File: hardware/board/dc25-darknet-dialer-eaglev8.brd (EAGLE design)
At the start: 101.6 x 101.6 mm, 80 parts, among them SW1 RESET, X1 USB-MICROB, Y1 RESONATORSMD

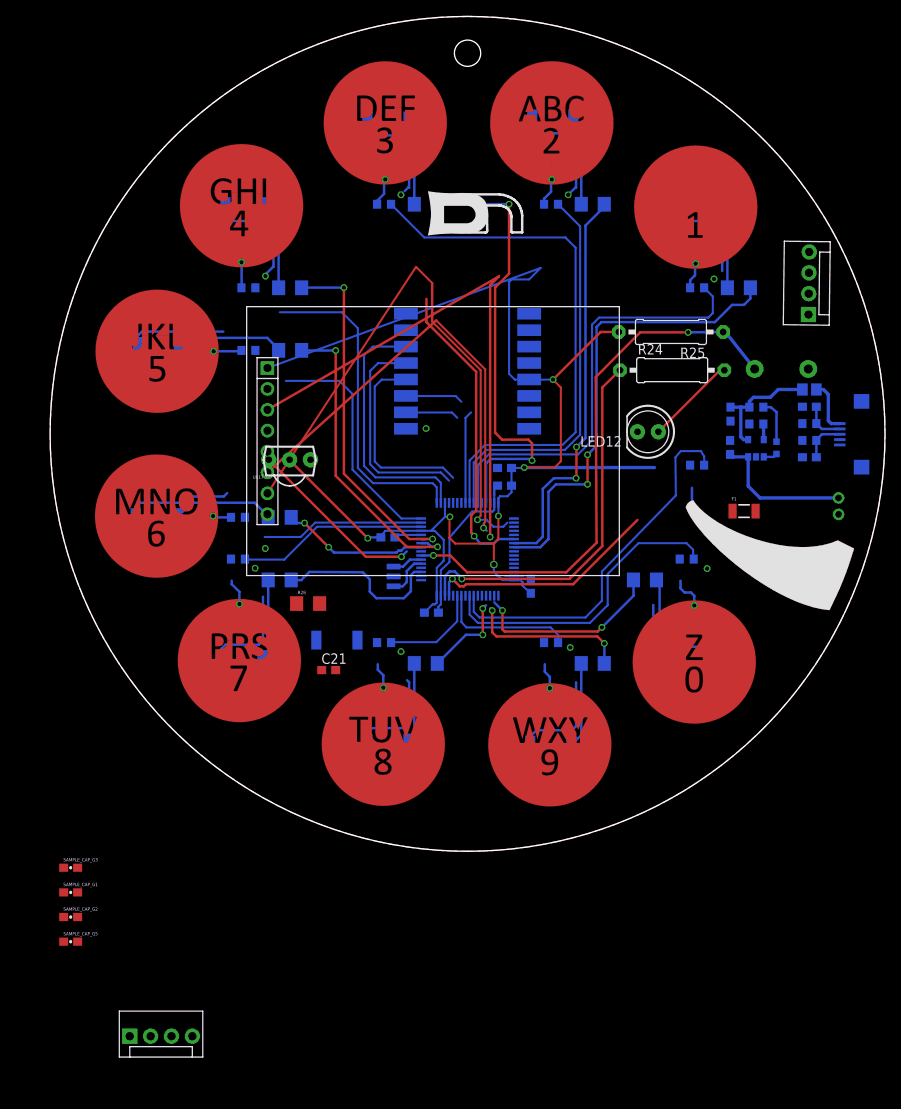
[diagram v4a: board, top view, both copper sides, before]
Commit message: Cleanup and update of schematic, added voltage regulator
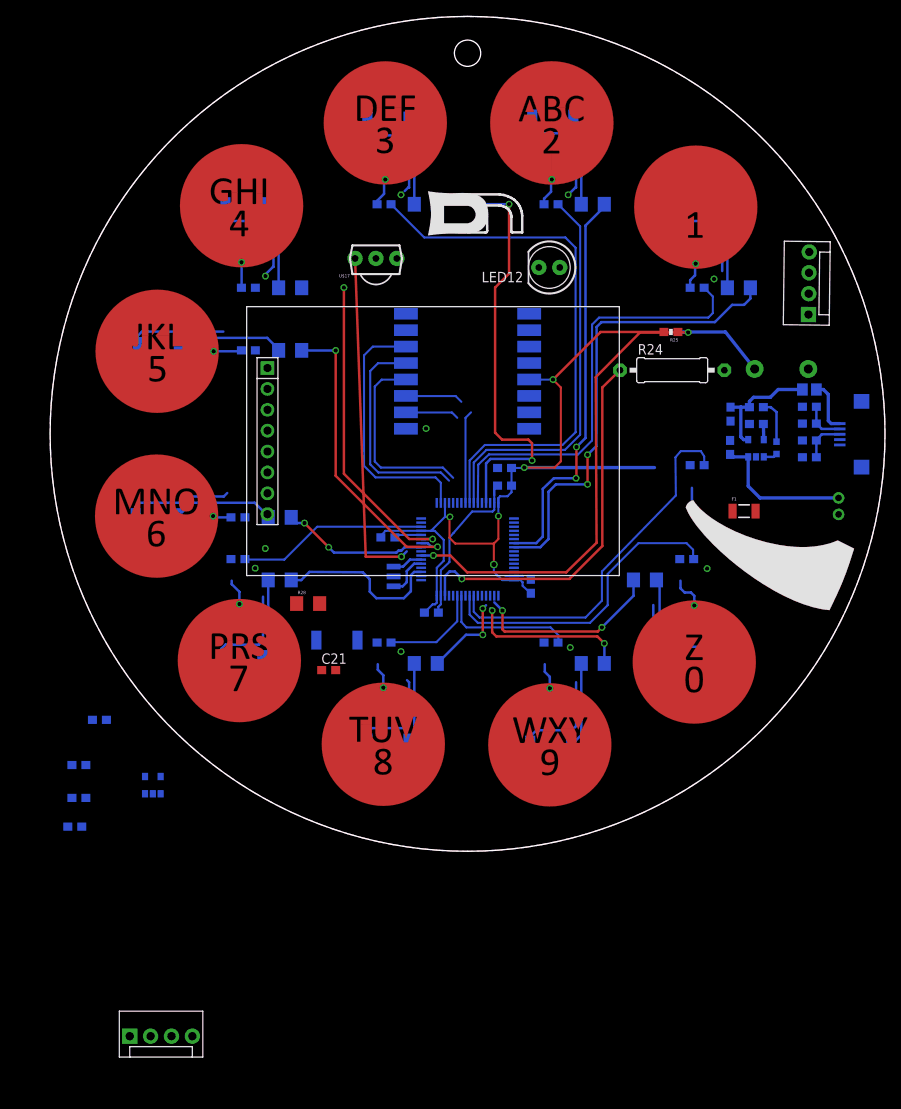
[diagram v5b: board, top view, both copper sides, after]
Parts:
- added U$19: TLV702, darknet_parts_library:SOT23-5
- C12, C13, C14: value 100nF -> 0.1uF; device SYNShop:C0603 -> darknet_parts_library:C0603
- C15: value 10nF -> 0.01uF; device SYNShop:C0603 -> darknet_parts_library:C0603
- C16, C17, C18: device SYNShop:C0603 -> darknet_parts_library:C0603
- C19, C20: value (none) -> 47pF; device SYNShop:C0603 -> darknet_parts_library:C0603
- C21: value (none) -> 1uF; device SYNShop:C0603 -> darknet_parts_library:C0603
- R1, R10, R2, R28, R3, R4, R5, R6, R7, R8, R9: device SYNShop:1206 -> darknet_parts_library:1206
- R11, R12, R13, R14, R15, R16, R17, R18, R19, R20, R21, R22, R23: device SYNShop:R0603 -> darknet_parts_library:0603-RES
- R24: device SYNShop:0309/12 -> darknet_parts_library:0309/12
- R25: device SYNShop:0309/12 -> darknet_parts_library:0603-RES
- R26, R27: value (none) -> 27; device SYNShop:R0603 -> darknet_parts_library:0603-RES
- SAMPLE_CAP_G1, SAMPLE_CAP_G2, SAMPLE_CAP_G3, SAMPLE_CAP_G5: value 10pF -> 0.047uF; device SparkFun-Capacitors:0603-CAP -> darknet_parts_library:C0603
- X1: value USB-MICROB -> 10118193-0001LF
- moved U$17 26.7 mm to (39.6, 72.2)
- moved LED12 23.3 mm to (60.8, 71.0)
- moved SAMPLE_CAP_G3 18.3 mm to (6.00, 16.0), flipped to the bottom
- moved SAMPLE_CAP_G1 15.5 mm to (3.50, 10.5), flipped to the bottom
- moved SAMPLE_CAP_G2 14.5 mm to (3.50, 6.50), flipped to the bottom
- moved SAMPLE_CAP_G5 14.0 mm to (3.00, 3.00), flipped to the bottom
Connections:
- removed net N$31: F1.2
- new net N$30: F1.2, U$19.1, U$19.3
- net GND: now also SAMPLE_CAP_G1.2, SAMPLE_CAP_G2.2, SAMPLE_CAP_G3.2, SAMPLE_CAP_G5.2, U$19.2
- net USB_DM: now also R26.2
- net USB_DP: now also R27.2
- net VCC: now also U$19.5
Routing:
- net LCD_SPI_SCK: track 71.3 -> 0.00 mm, vias 1 -> 0
- net LCD_SPI_NSS: track 65.0 -> 0.00 mm, vias 1 -> 0
- net VCC: track 166.2 -> 102.7 mm, vias 6 -> 5
- net LCD_SPI_MOSI: track 56.0 -> 0.00 mm, vias 1 -> 0
- net TSC_G1_IO4: track 39.8 -> 0.00 mm
- net LCD_RESET: track 37.3 -> 0.00 mm, vias 1 -> 0
- net TSC_G1_IO3: track 28.8 -> 0.00 mm
- net TIM_IR_CARRIER_FREQ: track 28.5 -> 0.00 mm, vias 1 -> 0
- net TSC_G1_IO2: track 19.8 -> 0.00 mm
- net IR_RCV: track 21.9 -> 41.6 mm
- net N$23: track 11.1 -> 0.00 mm
- net LED4: track 43.3 -> 38.2 mm
- net RESET: track 67.6 -> 70.1 mm

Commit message: Updated display module, added antenna design
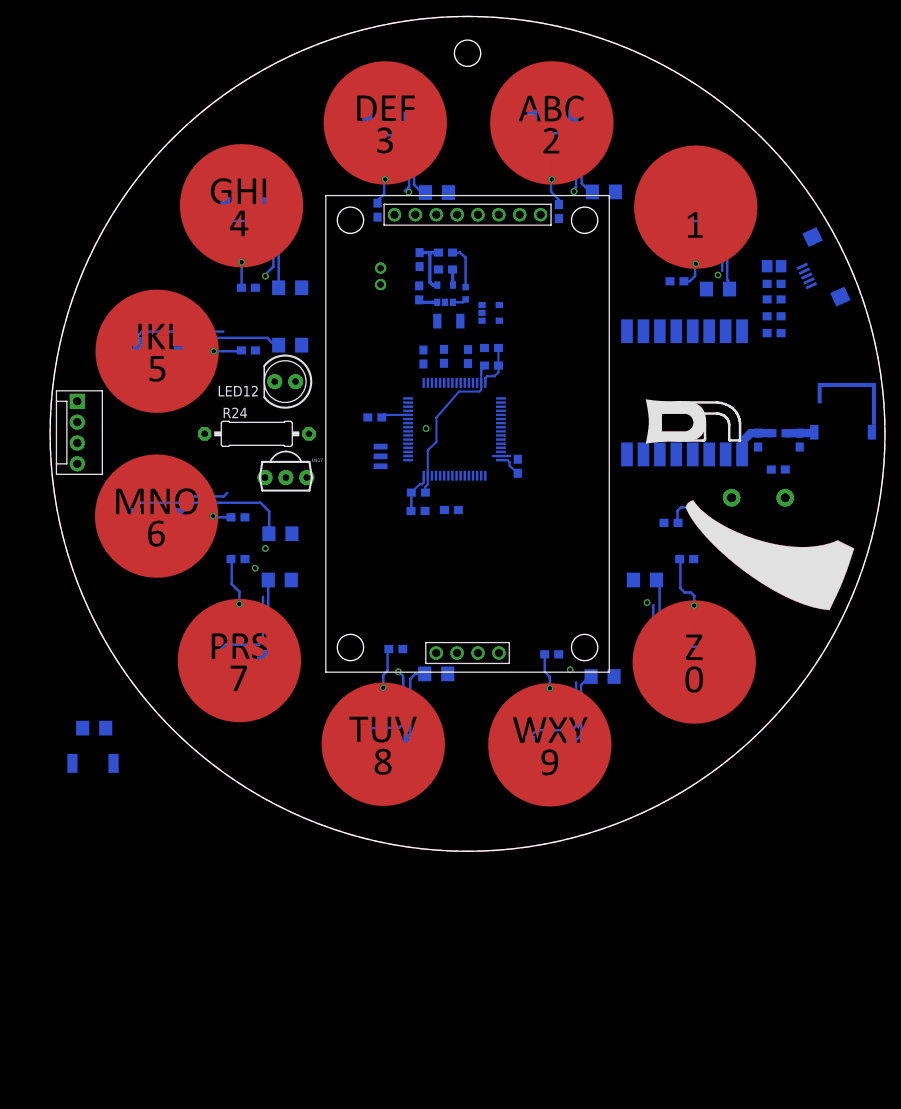
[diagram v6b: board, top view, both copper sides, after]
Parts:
- removed SD_CARD_HEADER: SD_CARD_HEADER, darknet_parts_library:SD_CARD_CONNECTOR
- removed U$12: COLOR_LCD_MODULE, darknet_parts_library:COLOR_LCD_DISPLAY
- added C1: 0.5pF, darknet_parts_library:C0603
- added L2: 10nH, darknet_parts_library:0603
- added L3: 4.7nH, darknet_parts_library:0603
- added U$21: CHIP_ANTENNA, darknet_parts_library:CHIP_ANTENNA_1.8X8MM
- added U$22: ST7735S_LCD_MODULE, darknet_parts_library:ST7735S_LCD_DISPLAY
- moved STLINK 91.4 mm to (3.31, 49.7), turned to 270 degrees
- moved U$19 70.7 mm to (53.6, 65.5), turned to 90 degrees
- moved SAMPLE_CAP_G2 69.7 mm to (47.9, 60.2), turned to 90 degrees
- moved SAMPLE_CAP_G1 65.0 mm to (45.4, 60.2), turned to 90 degrees
- moved SAMPLE_CAP_G3 63.0 mm to (50.8, 60.2), turned to 90 degrees
- moved CN1 62.4 mm to (40.2, 70.0)
- moved SAMPLE_CAP_G5 59.9 mm to (48.8, 41.5), turned to 180 degrees
- moved R24 51.1 mm to (25.1, 50.8)
- moved F1 42.7 mm to (48.5, 64.5), flipped to the bottom, turned to 180 degrees
- moved U$11 42.3 mm to (48.1, 67.8)
- moved C17 42.3 mm to (44.9, 68.0)
- moved LED11 42.3 mm to (50.6, 67.9)
- moved R22 42.3 mm to (48.1, 70.8)
- moved R23 42.3 mm to (48.1, 72.9)
- moved C18 42.3 mm to (45.0, 72.0)
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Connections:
- new net ANT: L2.1, L3.2, U$15.ANT
- new net N$31: C1.2, L2.2, U$21.P$1
- net GND: now also C1.1, L3.1, U$22.GND; no longer U$12.GND
- net LCD_BACK_LIT: now also U$22.LED; no longer U$12.LED
- net LCD_DATA_CMD: now also U$22.A0; no longer U$12.A0
- net LCD_RESET: now also U$22.RESET; no longer U$12.RESET
- net LCD_SPI_MOSI: now also U$22.SDA; no longer U$12.SDA
- net LCD_SPI_NSS: now also U$22.CS; no longer U$12.CS
- net LCD_SPI_SCK: now also U$22.SCK; no longer U$12.SCK
- net RFM69_SPI_MISO: now also U$22.SD_MISO; no longer SD_CARD_HEADER.SD_MISO
- net RFM69_SPI_MOSI: now also U$22.SD_MOSI; no longer SD_CARD_HEADER.SD_MOSI
- net RFM69_SPI_SCK: now also U$22.SD_SCK; no longer SD_CARD_HEADER.SD_SCK
- net SD_CS: now also U$22.SD_CS; no longer SD_CARD_HEADER.SD_CS
- net VCC: now also U$22.VCC; no longer U$12.VCC
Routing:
- net VCC: track 102.7 -> 13.5 mm, vias 5 -> 0
- net RESET: track 70.1 -> 0.00 mm, vias 2 -> 0
- net TSC_G3_IO1: track 66.6 -> 0.00 mm
- net LED1: track 56.6 -> 0.00 mm, vias 2 -> 0
- net LED3: track 55.1 -> 0.00 mm, vias 2 -> 0
- net TSC_G3_IO3: track 52.6 -> 0.00 mm
- net LED2: track 49.0 -> 0.00 mm, vias 2 -> 0
- net TSC_G3_IO2: track 48.4 -> 0.00 mm
- net IR_OUT: track 46.1 -> 0.00 mm, vias 1 -> 0
- net TSC_G5_IO1: track 45.1 -> 0.00 mm
- net IR_RCV: track 41.6 -> 0.00 mm, vias 1 -> 0
- net LED4: track 38.2 -> 0.03 mm, vias 2 -> 0
- net TSC_G5_IO2: track 37.7 -> 0.00 mm
- net LED5: track 37.6 -> 0.00 mm, vias 2 -> 0
- net RFM69_RESET: track 31.6 -> 0.00 mm
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
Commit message: Changed status LED for board debugging
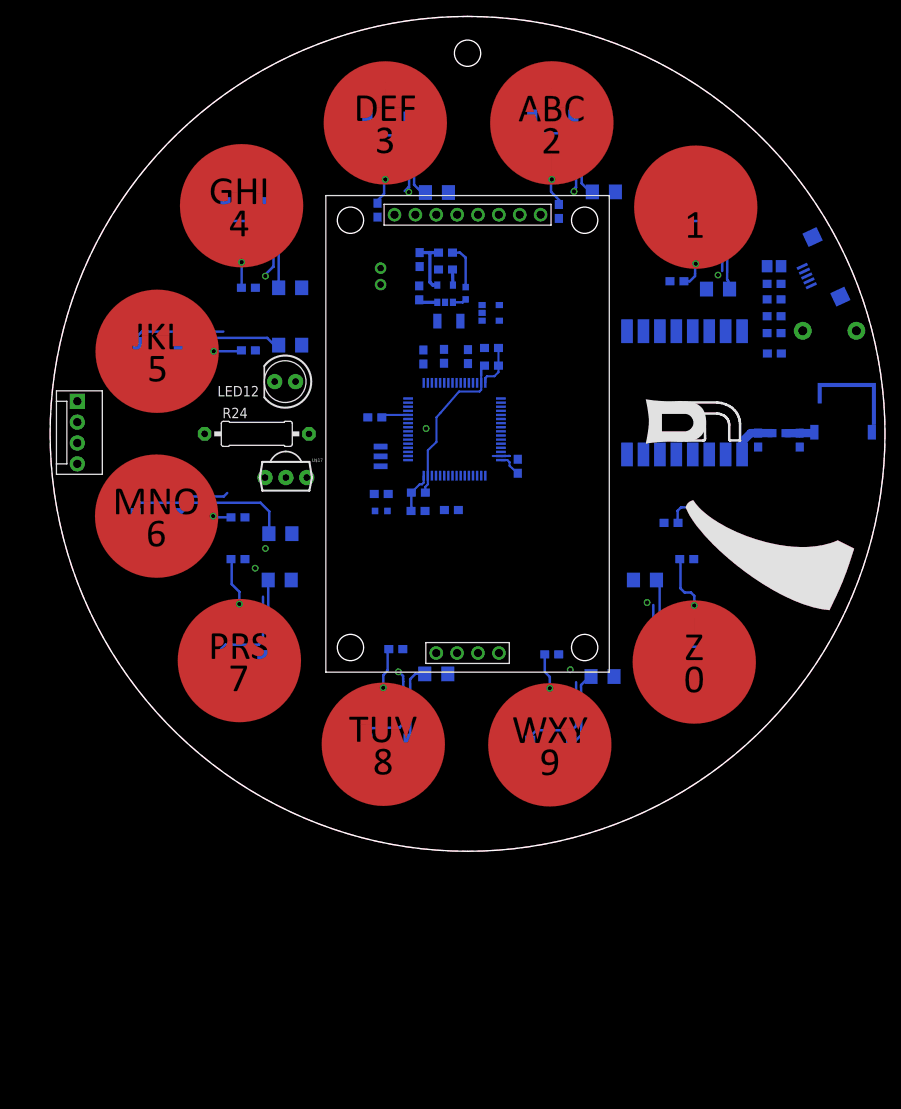
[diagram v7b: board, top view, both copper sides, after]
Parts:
- LED13: device SYNShop:GULLWING_LED -> SYNShop:LED-0603
- R28: device darknet_parts_library:1206 -> darknet_parts_library:0603-RES
- moved R28 45.1 mm to (40.3, 43.5)
- moved LED13 43.8 mm to (40.3, 41.4), turned to 90 degrees
- moved SW1 22.1 mm to (94.9, 63.3), turned to 0 degrees
- moved R25 14.1 mm to (88.1, 60.6)
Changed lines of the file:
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@@
 <element name="R24" library="darknet_parts_library" package="0309/12" value="" x="25.15" y="50.801875"/>
 <element name="CN1" library="adafruit" package="JST-PH-2-THM-RA" value="" x="40.218125" y="69.965" rot="MR270"/>
-<element name="SW1" library="SYNShop" package="TACTILE-2PIN-NARROW" value="RESET" x="86.19875" y="43.020625" rot="MR180"/>
-<element name="R25" library="darknet_parts_library" package="0603-RES" value="" x="88.609375" y="46.458125" rot="MR0"/>
+<element name="SW1" library="SYNShop" package="TACTILE-2PIN-NARROW" value="RESET" x="94.855625" y="63.341875" rot="MR0"/>
+<element name="R25" library="darknet_parts_library" package="0603-RES" value="" x="88.133125" y="60.586875" rot="MR0"/>
 <element name="R26" library="darknet_parts_library" package="0603-RES" value="27" x="88.10375" y="67.16375" rot="MR0"/>
 <element name="R27" library="darknet_parts_library" package="0603-RES" value="27" x="88.10375" y="65.11375" rot="MR0"/>
@@
 <element name="F1" library="SparkFun" package="PTC-1206" value="500uA" x="48.524375" y="64.525" rot="MR180"/>
 <element name="C21" library="darknet_parts_library" package="C0603" value="1uF" x="44.774375" y="41.4175" rot="MR0"/>
-<element name="LED13" library="SYNShop" package="GULLWING_LED" value="" x="7.71375" y="12.198125" rot="MR0"/>
-<element name="R28" library="darknet_parts_library" package="1206" value="" x="5.365" y="14.989375" rot="MR0"/>
+<element name="LED13" library="SYNShop" package="LED-0603" value="" x="40.296875" y="41.419375" rot="MR90"/>
+<element name="R28" library="darknet_parts_library" package="0603-RES" value="" x="40.29" y="43.485" rot="MR0"/>
 <element name="STLINK" library="darknet_parts_library" package="1X04" value="STLINK-V2-CONNECTOR" x="3.306875" y="49.688125" rot="R270"/>
 <element name="SAMPLE_CAP_G3" library="darknet_parts_library" package="C0603" value="0.047uF" x="50.845625" y="60.19875" rot="MR90"/>
@@
 <wire x1="42.95775" y1="21.336" x2="42.306875" y2="21.986875" width="0.3048" layer="16"/>
 <wire x1="42.306875" y1="21.986875" x2="42.306875" y2="22.06625" width="0.3048" layer="16"/>
-<wire x1="20.828" y1="23.344" x2="7.71375" y2="10.698125" width="0" layer="19" extent="16-16"/>
 </signal>
 <signal name="N$1">
@@
 <contactref element="R25" pad="1"/>
 <contactref element="SW1" pad="P$1"/>
-<wire x1="89.46265" y1="43.020625" x2="89.459375" y2="46.458125" width="0" layer="19" extent="16-16"/>
-<wire x1="43.5625" y1="50.605" x2="89.459375" y2="46.458125" width="0" layer="19" extent="16-16"/>
+<wire x1="88.983125" y1="60.586875" x2="91.591725" y2="63.341875" width="0" layer="19" extent="16-16"/>
+<wire x1="43.5625" y1="50.605" x2="88.983125" y2="60.586875" width="0" layer="19" extent="16-16"/>
 </signal>
 <signal name="VCC">
@@
 <wire x1="43.9625" y1="43.655" x2="43.9625" y2="41.455625" width="0.3048" layer="16"/>
 <wire x1="43.9625" y1="41.455625" x2="43.924375" y2="41.4175" width="0.3048" layer="16"/>
-<wire x1="54.66125" y1="64.575625" x2="59.69" y2="77.47" width="0" layer="19" extent="16-16"/>
-<wire x1="54.5625" y1="61.255" x2="54.66125" y2="64.575625" width="0" layer="19" extent="16-16"/>
+<wire x1="76.205" y1="48.295" x2="87.283125" y2="60.586875" width="0" layer="19" extent="16-16"/>
+<wire x1="56.9125" y1="46.005" x2="76.205" y2="48.295" width="0" layer="19" extent="16-16"/>
+<wire x1="52.9625" y1="57.005" x2="54.8625" y2="47.605" width="0" layer="19" extent="16-16"/>
+<wire x1="54.66125" y1="64.575625" x2="54.5625" y2="61.255" width="0" layer="19" extent="16-16"/>
 <wire x1="46.4625" y1="57.005" x2="52.9625" y2="57.005" width="0" layer="19" extent="16-16"/>
 <wire x1="43.5625" y1="53.605" x2="46.4625" y2="57.005" width="0" layer="19" extent="16-16"/>
 <wire x1="38.6625" y1="52.805" x2="43.5625" y2="53.605" width="0" layer="19" extent="16-16"/>
 <wire x1="45.4625" y1="45.705" x2="43.5625" y2="53.605" width="0" layer="19" extent="16-16"/>
-<wire x1="54.8625" y1="47.605" x2="52.9625" y2="57.005" width="0" layer="19" extent="16-16"/>
 <wire x1="28.691875" y1="45.48375" x2="38.6625" y2="52.805" width="0" layer="19" extent="16-16"/>
-<wire x1="76.205" y1="48.295" x2="56.9125" y2="46.005" width="0" layer="19" extent="16-16"/>
-<wire x1="87.759375" y1="46.458125" x2="76.205" y2="48.295" width="0" layer="19" extent="16-16"/>
+<wire x1="59.69" y1="77.47" x2="54.66125" y2="64.575625" width="0" layer="19" extent="16-16"/>
 <wire x1="3.306875" y1="54.768125" x2="28.691875" y2="45.48375" width="0" layer="19" extent="1-1"/>
 </signal>
@@
 <contactref element="U$2" pad="P2"/>
 <contactref element="R28" pad="1"/>
-<wire x1="6.765" y1="14.989375" x2="43.5625" y2="48.105" width="0" layer="19" extent="16-16"/>
+<wire x1="41.14" y1="43.485" x2="43.5625" y2="48.105" width="0" layer="19" extent="16-16"/>
 </signal>
 <signal name="TSC_G5_IO4">
@@
 <contactref element="LED13" pad="A"/>
 <contactref element="R28" pad="2"/>
-<wire x1="2.71375" y1="10.698125" x2="3.965" y2="14.989375" width="0" layer="19" extent="16-16"/>
+<wire x1="39.546875" y1="41.419375" x2="39.44" y2="43.485" width="0" layer="19" extent="16-16"/>
 </signal>
 <signal name="TSC_G2_I01">

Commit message: Finished routing
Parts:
- added U$12: KRUX_LOGO, darknet_parts_library:KRUX_LOGO
- added U$23: CMD_C0DE_LOGO, darknet_parts_library:CMD_C0DE_LOGO
- R24: device darknet_parts_library:0309/12 -> darknet_parts_library:0207/7
- U$17: device SYNShop:IR-MODULE -> darknet_parts_library:IR-MODULE
- moved R10 3.99 mm to (75.8, 35.1)
- moved R24 3.60 mm to (28.7, 51.4), turned to 180 degrees
- moved R20 3.17 mm to (75.8, 32.9), turned to 180 degrees
- moved R17 2.46 mm to (22.8, 33.1)
- moved R6 1.99 mm to (27.9, 40.6)
- moved U$19 1.85 mm to (53.9, 67.4)
- moved LED11 1.83 mm to (50.6, 69.7)
- moved U$11 1.83 mm to (48.1, 69.6)
- moved C17 1.83 mm to (45.0, 69.8)
- moved C18 1.83 mm to (45.0, 73.8)
- moved R22 1.83 mm to (48.2, 72.6)
- moved R23 1.83 mm to (48.2, 74.7)
- moved F1 1.83 mm to (48.6, 66.4)
- moved C15 1.16 mm to (38.4, 53.2), turned to 180 degrees
- moved LED12 0.39 mm to (28.7, 57.5), turned to 0 degrees
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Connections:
- net TSC_G2_I03 renamed TSC_G2_IO3
- removed net TSC_G2_I01: R18.1, U$2.P20
- removed net TSC_G2_I02: R17.1, U$2.P21
- new net TSC_G2_IO1: R14.1, U$2.P20
- new net TSC_G2_IO2: R15.1, U$2.P21
- net GND: now also CN1.2; no longer CN1.1
- net TSC_G1_IO1: now also R18.1; no longer R16.1
- net TSC_G1_IO2: now also R17.1; no longer R15.1
- net TSC_G1_IO3: now also R16.1; no longer R14.1
- net VCC1: now also CN1.1; no longer CN1.2
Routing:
- net VCC: track 13.5 -> 167.9 mm, vias 0 -> 7
- net RFM69_SPI_SCK: track 0.00 -> 67.1 mm, vias 0 -> 3
- net RESET: track 0.00 -> 64.5 mm, vias 0 -> 2
- net RFM69_SPI_MOSI: track 0.00 -> 64.0 mm, vias 0 -> 1
- net SYS_JTMS_SWDIO: track 0.00 -> 63.4 mm, vias 0 -> 1
- net TSC_G1_IO1: track 0.00 -> 63.1 mm
- net RFM69_SPI_MISO: track 0.00 -> 62.5 mm, vias 0 -> 1
- net VCC0: track 6.94 -> 68.5 mm, vias 0 -> 2
- net SYS_JTCK-SWCLK: track 0.00 -> 53.6 mm, vias 0 -> 1
- net RFM69_RESET: track 0.00 -> 52.8 mm, vias 0 -> 2
- net USB_DM: track 0.00 -> 49.8 mm
- net USB_DP: track 0.00 -> 49.4 mm
- net TSC_G1_IO2: track 0.00 -> 46.9 mm
- net LED3: track 0.00 -> 45.5 mm, vias 0 -> 2
- net RFM69_SPI_NSS: track 0.00 -> 43.2 mm, vias 0 -> 2
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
